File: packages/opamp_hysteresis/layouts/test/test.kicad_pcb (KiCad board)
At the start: 2 copper layers, 4 parts, among them U1 BW CMRR Ib Vos GBW Iout SR

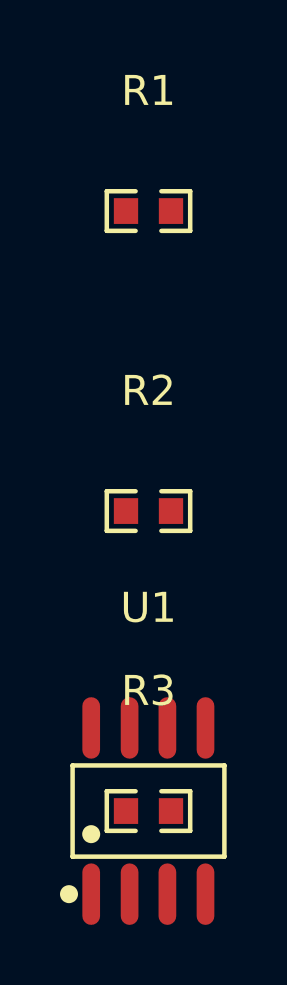
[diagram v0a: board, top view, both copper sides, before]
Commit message: opamp: improve calc, still needs fix
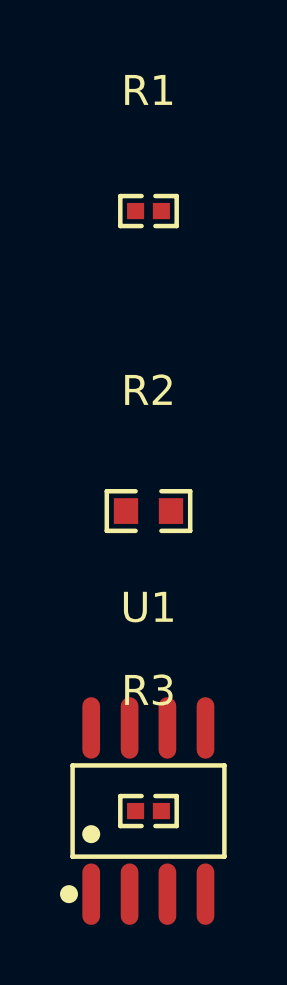
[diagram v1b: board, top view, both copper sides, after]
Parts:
- R1, R3: value 10kΩ ±1% 100mW -> 50kΩ ±1% 62.5mW; footprint UNI_ROYAL_0603WAF1002T5E:R0603 -> RALEC_RTT025002FTH:R0402
